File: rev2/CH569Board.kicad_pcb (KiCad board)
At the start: 4 copper layers, 47.3 x 49.6 mm, 35 parts, among them CN1 BA42-80BT-1-NHB, J1 Conn_01x02_Male, J2 Conn_01x03_Male, U1 AMS1117-3.3, U4 CH569W, X1 O705030MEEA4SC

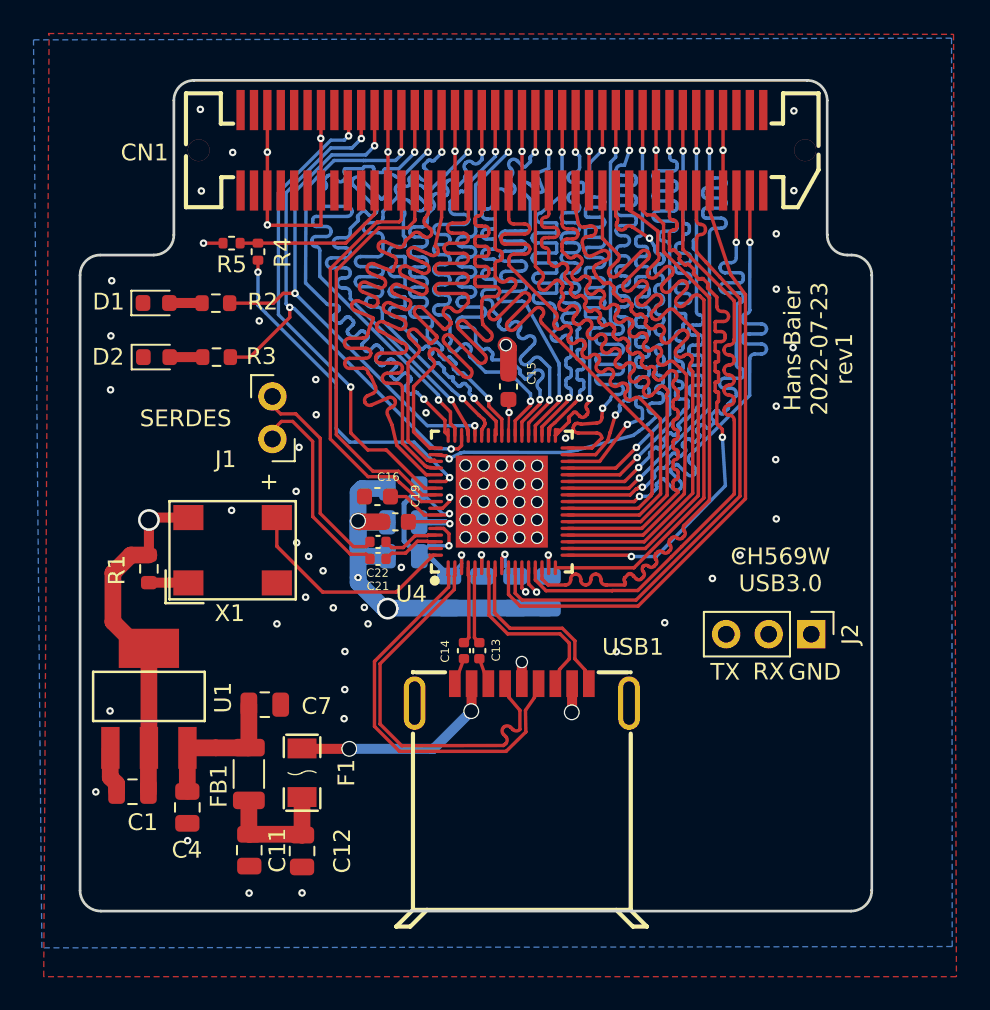
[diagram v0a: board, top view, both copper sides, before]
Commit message: fix high speed tracks, move crystal closer, clean up power supply traces
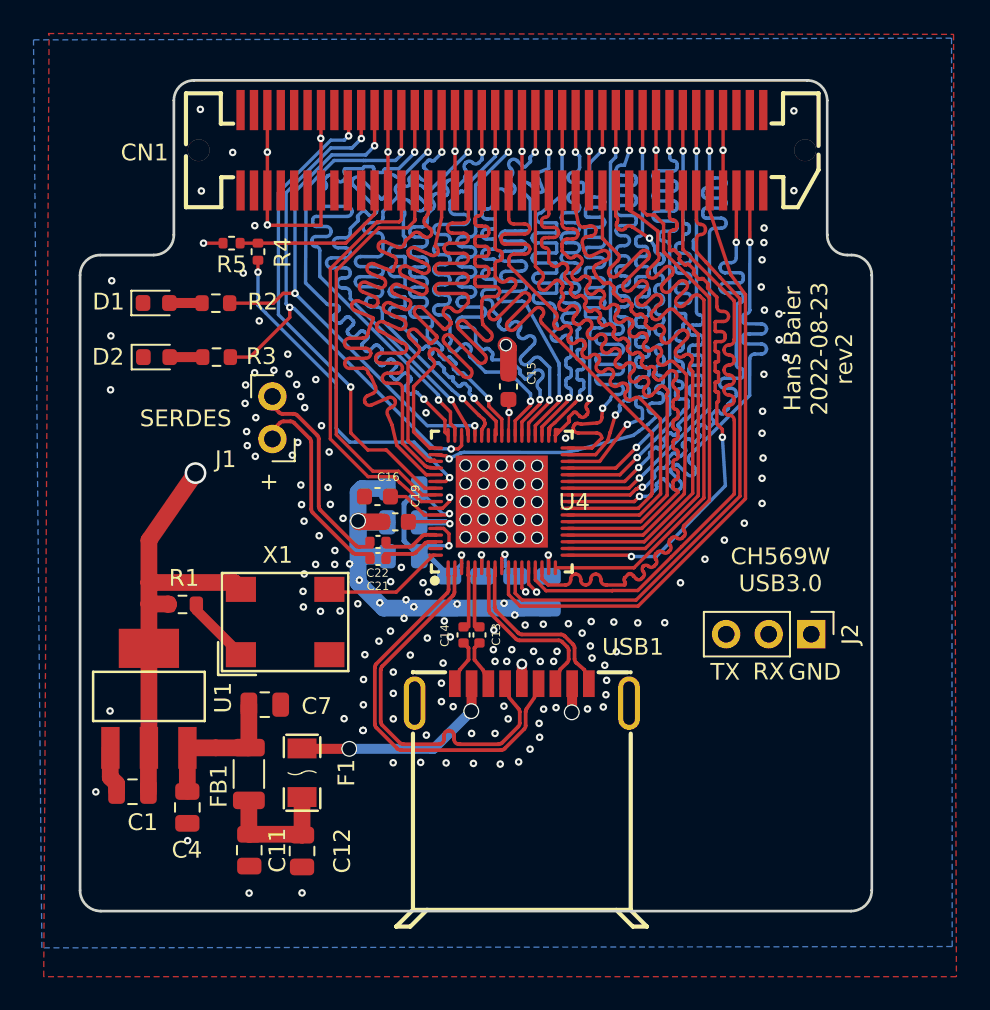
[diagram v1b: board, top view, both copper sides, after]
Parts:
- moved X1 5.31 mm to (112.7, 110.5)
- moved R1 2.92 mm to (106.5, 109.5), turned to 0 degrees
- moved C14 0.94 mm to (123.3, 111.3)
- moved C13 0.94 mm to (124.3, 111.3)
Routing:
- net /XI: track 13.2 -> 7.66 mm
- net +3V3: track 91.7 -> 93.7 mm
- net Net-(R1-Pad2): track 2.36 -> 4.10 mm
- net /STDA_SSTX-: track 1.58 -> 2.80 mm
- net /STDA_SSTX+: track 1.59 -> 2.80 mm
- net /SSTX+: track 4.60 -> 3.53 mm
- net /SSTX-: track 4.60 -> 3.53 mm
- net GND: track 80.6 -> 80.4 mm, vias 84 -> 182
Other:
- board text added: "Hans Baier 2022-08-23"
- board text added: "rev2"
- board text removed: "Hans Baier 2022-07-23"
- board text removed: "rev1"

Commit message: Some finishes. Put OSHW logo on silkscreen
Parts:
- added N1: OHWLOGO, Symbols:OSHW-Symbol_6.7x6mm_SilkScreen, F.Cu at (140.1, 118.6)
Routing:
- net GND: track 80.4 -> 82.1 mm, vias 182 -> 186

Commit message: redo power section with different LDO, add decoupling cap and reset switch
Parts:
- added C2: 1uF, Capacitor_SMD:C_0805_2012Metric, F.Cu at (102.3, 113.7)
- added C3: 1uF, Capacitor_SMD:C_0805_2012Metric, F.Cu at (106.7, 115.5)
- added C5: 100nF, Capacitor_SMD:C_0402_1005Metric, F.Cu at (110.1, 106.8)
- added R6: 10k, Resistor_SMD:R_0402_1005Metric, F.Cu at (105.9, 118.8)
- added SW1: TS-1187A-B-A-B, easyeda2kicad:SW-SMD_4P-L5.1-W5.1-P3.70-LS6.5-TL-2, F.Cu at (104.3, 101.7)
- U1: value AMS1117-3.3 -> SPX3819M5-L-3-3/TR; footprint easyeda2kicad:SOT-223-3_L6.5-W3.4-P2.30-LS7.0-BR -> easyeda2kicad:SOT-23-5_L3.0-W1.7-P0.95-LS2.8-BR
- moved C1 8.70 mm to (105.5, 112.2), turned to 180 degrees
- moved U1 3.64 mm to (103.2, 118.5)
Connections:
- U1 pad 1: GND -> +5V
- U1 pad 2: +3V3 -> GND
- U1 pad 3: +5V -> Net-(R6-Pad1)
- U1 pad 4: +3V3 -> Net-(C3-Pad1)
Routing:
- net Net-(R6-Pad1): track 0.00 -> 22.8 mm, vias 0 -> 2
- net GND: track 82.1 -> 92.6 mm, vias 186 -> 227
- net +5V: track 8.84 -> 15.3 mm
- net +3V3: track 93.3 -> 88.8 mm
- net Net-(C3-Pad1): track 0.00 -> 2.76 mm

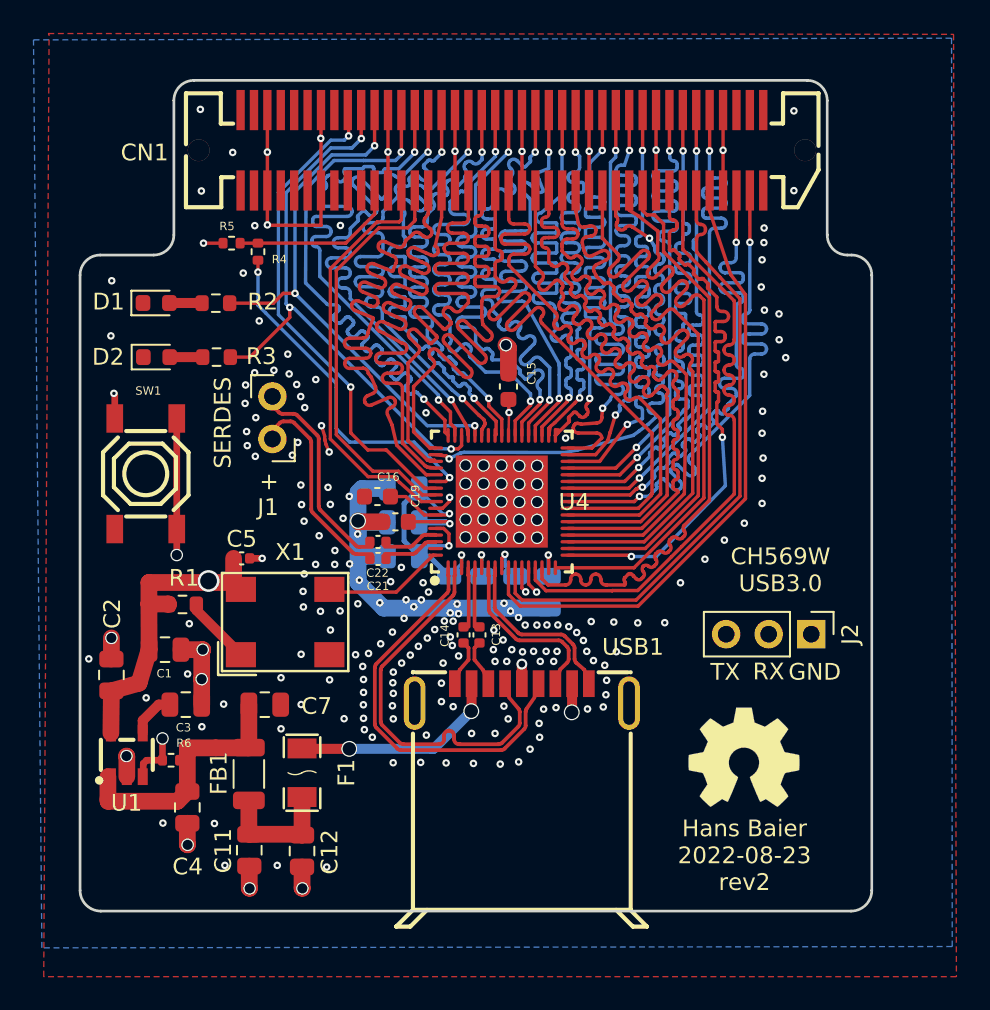
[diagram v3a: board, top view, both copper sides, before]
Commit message: stitch board edges and add more ground vias
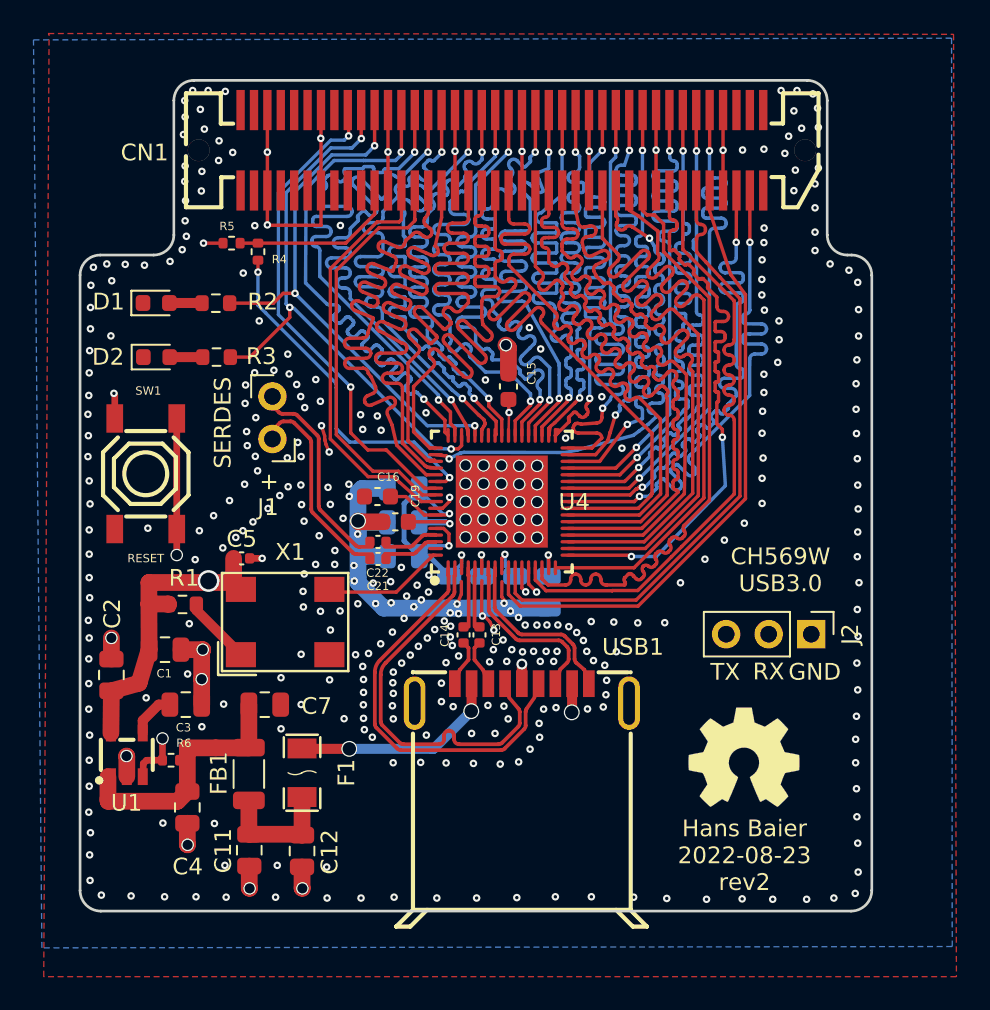
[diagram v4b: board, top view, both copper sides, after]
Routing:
- net GND: track 92.6 -> 98.5 mm, vias 227 -> 371

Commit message: rev2 ready for the fab. used a crystal instead of an XO, because of better specs
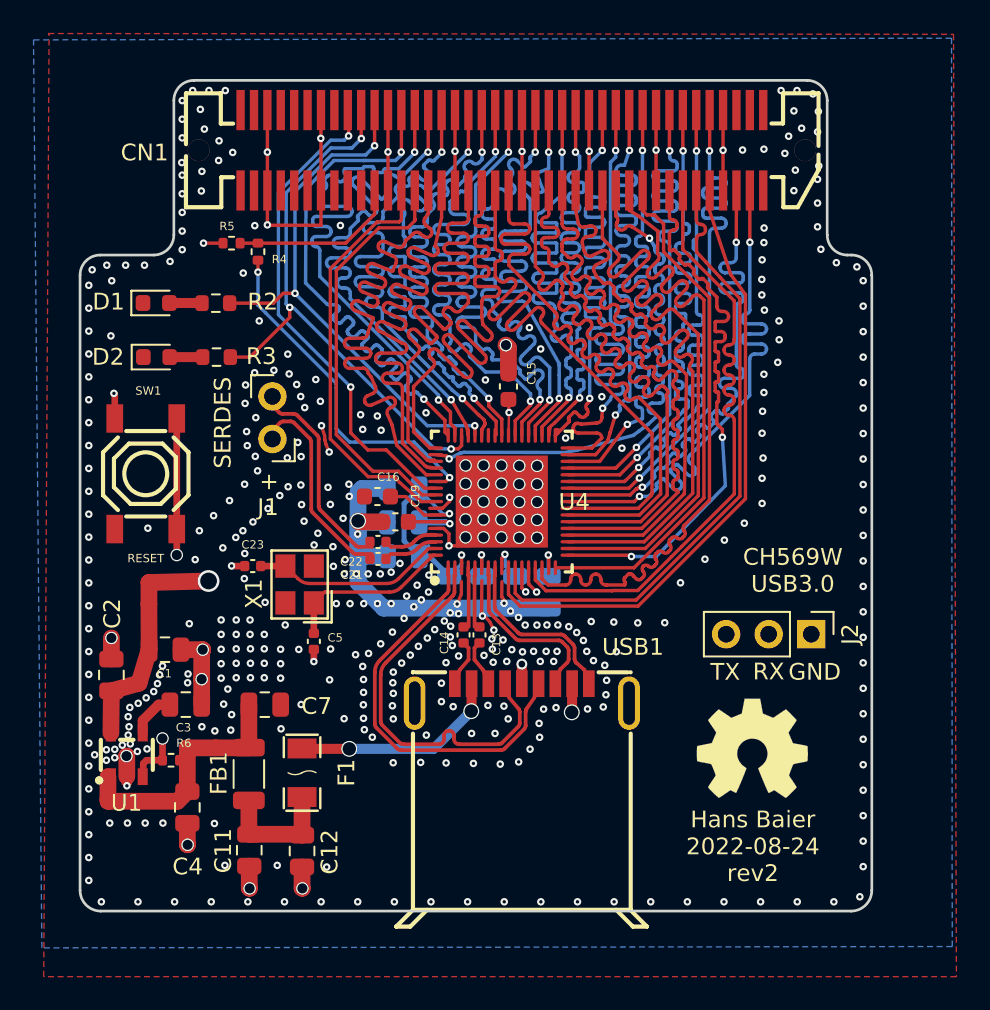
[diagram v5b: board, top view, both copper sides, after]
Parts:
- removed R1: 10k, Resistor_SMD:R_0603_1608Metric
- added C23: 10pF, Capacitor_SMD:C_0402_1005Metric, F.Cu at (110.7, 107.2)
- C5: value 100nF -> 10pF
- X1: value O705030MEEA4SC -> X1E0000210295; footprint easyeda2kicad:OSC-SMD_4P-L7.0-W5.0-BL -> easyeda2kicad:CRYSTAL-SMD_4P-L3.2-W2.5-BL
- moved C5 6.57 mm to (114.4, 111.7), turned to -90 degrees
- moved X1 2.40 mm to (113.5, 108.3), turned to 90 degrees
- moved N1 0.73 mm to (140.6, 118.1)
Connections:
- C5 pad 1: +3V3 -> /XI
- U4 pad 67: unconnected-(U4-Pad67) -> /XO
- X1 pad 1: Net-(R1-Pad2) -> /XI
- X1 pad 3: /XI -> /XO
- X1 pad 4: +3V3 -> GND
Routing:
- net /XO: track 0.00 -> 11.6 mm
- net +3V3: track 88.8 -> 83.4 mm
- net Net-(R1-Pad2): track 4.10 -> 0.00 mm
- net /XI: track 7.66 -> 10.2 mm
- net GND: track 98.5 -> 99.3 mm, vias 371 -> 425
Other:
- board text added: "Hans Baier 2022-08-24"
- board text added: "Trace Impedances calculated for JLC7628 stackup"
- board text removed: "Hans Baier 2022-08-23"
